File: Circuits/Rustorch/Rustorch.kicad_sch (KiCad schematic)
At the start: 0 parts

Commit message: (Rustorch) 回路図部品配置中
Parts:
- added BZ1: Buzzer, symbol Device:Buzzer
- added C1, C3: 0.1u, symbol Device:C_Small
- added C2: 47u, symbol Device:C_Polarized_Small
- added D1, D3, D4, D5: 1N4148, symbol Device:D_Small
- added D2: LED_POWER, symbol Device:LED_Small
- added J1: USB_C_Receptacle_USB2.0_16P, symbol Connector:USB_C_Receptacle_USB2.0_16P
- added J2: OLED_128x64_IIC, symbol Connector:Conn_01x04_Socket
- added Q1, Q2, Q3, Q4: 2SC1815, Package_TO_SOT_THT:TO-92_Inline, symbol Transistor_BJT:2SC1815
- added R1, R2, R4, R5, R6: 4.7k, symbol Device:R_Small
- added R10, R13, R14, R15, R16, R17, R18, R19: 330, symbol Device:R_Small
- added R3, R7, R8, R9: 10k, symbol Device:R_Small
- added SW1: RESET, symbol Switch:SW_Push
- added SW2: SW_UP, symbol Switch:SW_Push
- added SW3: SW_LEFT, symbol Switch:SW_Push
- added SW4: SW_RIGHT, symbol Switch:SW_Push
- added SW5: SW_DOWN, symbol Switch:SW_Push
- added SW6: SW_A, symbol Switch:SW_Push
- added SW7: SW_B, symbol Switch:SW_Push
- added SW8: BOOT, symbol Switch:SW_Push
- added SW9: SW_POWER (5P), symbol Switch:SW_Push_SPDT
- added U1: ESP32-C6-WROOM-1, PCM_Espressif:ESP32-C6-WROOM-1, symbol PCM_Espressif:ESP32-C6-WROOM-1
- added U2: BA033CC0T, Package_TO_SOT_THT:TO-220-3_Vertical, symbol Regulator_Linear:LF33_TO220
- added U3, U4, U5, U6: OSL10561-L*, Display_7Segment:7SegmentLED_LTS6760_LTS6780, symbol Display_Character:SM420561N
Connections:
- new net: C1.1, D1.1 (K), R3.2, SW9.2 (B), U2.1 (VI)
- new net: J1.B5 (CC2), R2.1
- new net: D2.2 (A), R3.1
- new net: BZ1.1 (+), R7.2
- new net: U1.1 (GND), U1.28 (GND), U1.29 (GND)
- new net: Q1.3 (B), R4.2
- new net: J1.A5 (CC1), R1.1
- new net 3V3: C2.1, C3.1, D1.2 (A), J2.2 (Pin_2), R5.2, R6.2, U2.3 (VO)
- new net GND: BZ1.2 (-), C1.2, C2.2, C3.2, D2.1 (K), J1.A1 (GND), J1.A12 (GND), J1.B1 (GND), J1.B12 (GND), J2.1 (Pin_1), Q1.1 (E), Q2.1 (E), Q3.1 (E), Q4.1 (E), R1.2, R2.2, U2.2 (GND)
- new net SCL: J2.3 (Pin_3), R6.1, U1.7 (MTDO/GPIO7)
- new net SDA: J2.4 (Pin_4), R5.1, U1.6 (MTCK/GPIO6/ADC1_CH6)
- new net USB_D+: J1.A6 (D+), J1.B6 (D+), U1.14 (GPIO13/USB_D+)
- new net USB_D-: J1.A7 (D-), J1.B7 (D-), U1.13 (GPIO12/USB_D-)
- new net VBUS: J1.A4 (VBUS), J1.A9 (VBUS), J1.B4 (VBUS), J1.B9 (VBUS), SW9.1 (A)
- no-connect marks 0 -> 4

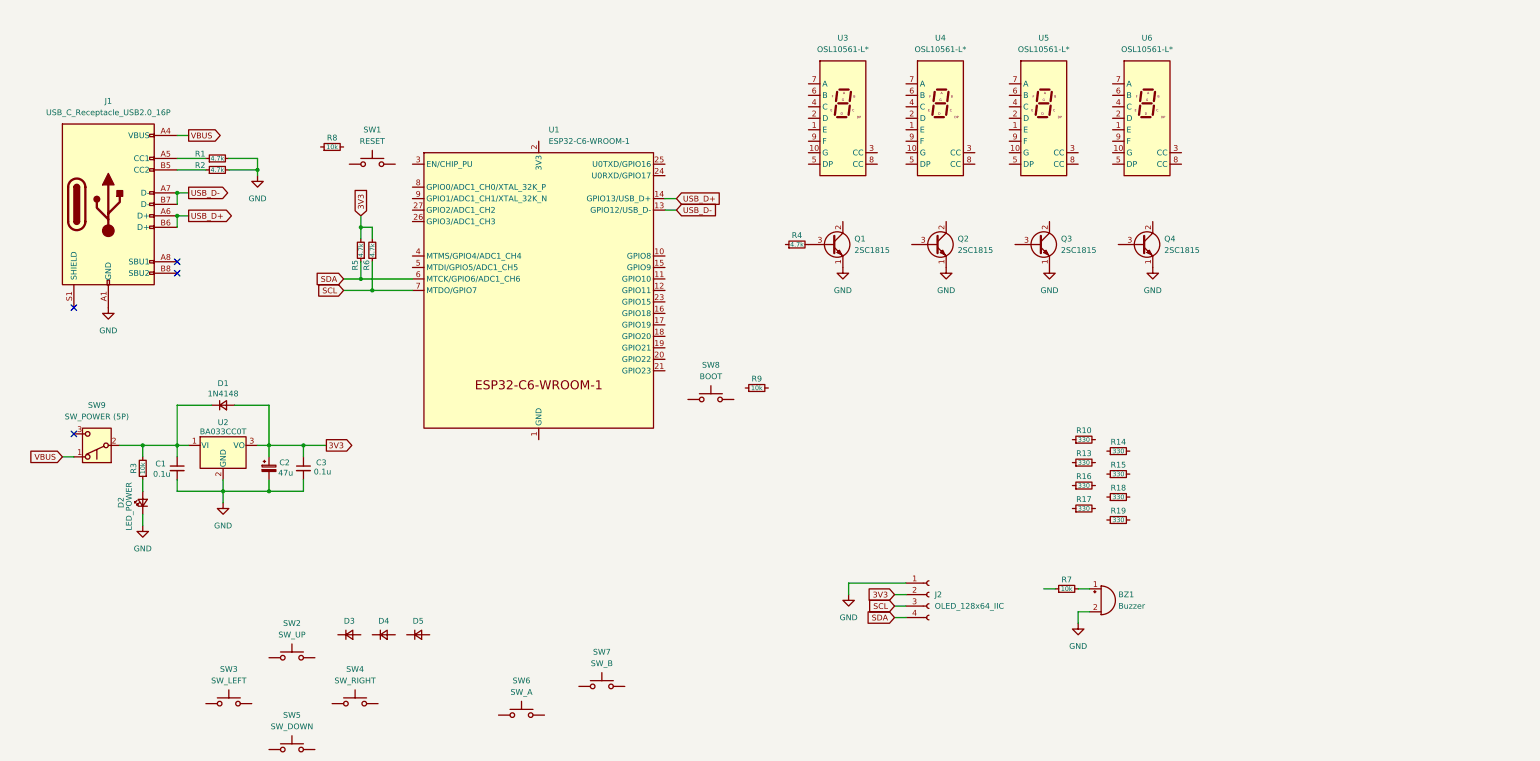
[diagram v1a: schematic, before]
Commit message: (Rustorch) 回路図修正 (7セグ部分追加)
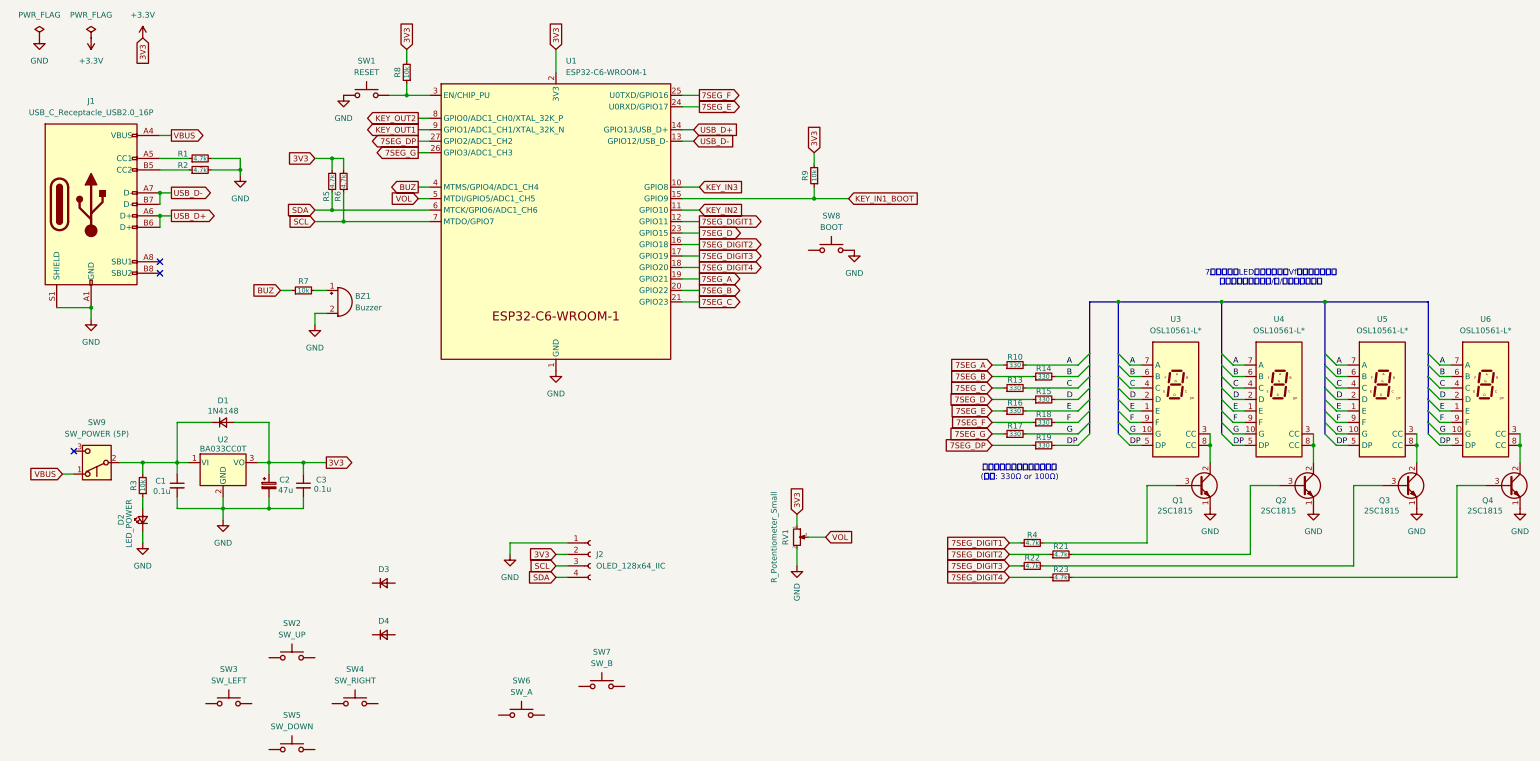
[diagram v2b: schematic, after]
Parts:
- removed D5: 1N4148, symbol Device:D_Small
- added R21, R22, R23: 4.7k, symbol Device:R_Small
- added RV1: R_Potentiometer_Small, symbol Device:R_Potentiometer_Small
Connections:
- net 3V3 is gone; now on net +3.3V: C2.1, C3.1, D1.2 (A), J2.2 (Pin_2), R5.2, R6.2, U2.3 (VO)
- net GND: now also J1.S1 (SHIELD), SW1.1, SW8.2, U1.1 (GND), U1.28 (GND), U1.29 (GND), RV1.3
- net at Q3.2 (C): now also U5.3 (CC), U5.8 (CC)
- net at Q3.3 (B): now also R22.2
- net at Q4.2 (C): now also U6.3 (CC), U6.8 (CC)
- net at Q4.3 (B): now also R23.2
- net E: now reaches U6.1 (E)
- net E: now also R16.2, U3.1 (E), U4.1 (E), U5.1 (E)
- net G: now reaches U6.10 (G)
- net G: now also R17.2, U3.10 (G), U4.10 (G), U5.10 (G)
- net D: now reaches U6.2 (D)
- net D: now also R15.2, U3.2 (D), U4.2 (D), U5.2 (D)
- net C: now reaches U6.4 (C)
- net C: now also R13.2, U3.4 (C), U4.4 (C), U5.4 (C)
- net DP: now reaches U6.5 (DP)
- net DP: now also R19.2, U3.5 (DP), U4.5 (DP), U5.5 (DP)
- net B: now reaches U6.6 (B)
- net B: now also R14.2, U3.6 (B), U4.6 (B), U5.6 (B)
- net A: now reaches U6.7 (A)
- net A: now also R10.2, U3.7 (A), U4.7 (A), U5.7 (A)
- net F: now reaches U6.9 (F)
- net F: now also R18.2, U3.9 (F), U4.9 (F), U5.9 (F)
- net 7SEG_G: now reaches R17.1
- net 7SEG_G: now also U1.26 (GPIO3/ADC1_CH3)
- net 7SEG_F: now reaches R18.1
- net 7SEG_F: now also U1.25 (U0TXD/GPIO16)
- net BUZ: now reaches R7.1
- net BUZ: now also U1.4 (MTMS/GPIO4/ADC1_CH4)
- net KEY_IN3: now reaches U1.10 (GPIO8)
- net KEY_IN2: now reaches U1.11 (GPIO10)
- net 7SEG_DIGIT1: now reaches U1.12 (GPIO11)
- net 7SEG_DIGIT1: now also R4.1
- net KEY_IN1_BOOT: now reaches U1.15 (GPIO9)
- net KEY_IN1_BOOT: now also R9.1
- net 7SEG_DIGIT2: now reaches U1.16 (GPIO18)
- net 7SEG_DIGIT2: now also R21.1
- net 7SEG_DIGIT3: now reaches U1.17 (GPIO19)
- net 7SEG_DIGIT3: now also R22.1
- net 7SEG_DIGIT4: now reaches U1.18 (GPIO20)
- net 7SEG_DIGIT4: now also R23.1
- net 7SEG_A: now reaches U1.19 (GPIO21)
- net 7SEG_A: now also R10.1
- net +3.3V: now reaches U1.2 (3V3)
- net +3.3V: now also R8.2, R9.2, RV1.1
- net 7SEG_B: now reaches U1.20 (GPIO22)
- net 7SEG_B: now also R14.1
- net 7SEG_C: now reaches U1.21 (GPIO23)
- net 7SEG_C: now also R13.1
- net 7SEG_D: now reaches U1.23 (GPIO15)
- net 7SEG_D: now also R15.1
- net 7SEG_E: now reaches U1.24 (U0RXD/GPIO17)
- net 7SEG_E: now also R16.1
- net 7SEG_DP: now reaches U1.27 (GPIO2/ADC1_CH2)
- net 7SEG_DP: now also R19.1
- net at U1.3 (EN/CHIP_PU): now also R8.1, SW1.2
- net VOL: now reaches U1.5 (MTDI/GPIO5/ADC1_CH5)
- net VOL: now also RV1.2
- net KEY_OUT2: now reaches U1.8 (GPIO0/ADC1_CH0/XTAL_32K_P)
- net KEY_OUT1: now reaches U1.9 (GPIO1/ADC1_CH1/XTAL_32K_N)
- net at Q1.2 (C): now also U3.3 (CC), U3.8 (CC)
- net at U4.3 (CC): now also Q2.2 (C), U4.8 (CC)
- net at Q2.3 (B): now also R21.2
- no-connect marks 4 -> 3
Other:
- note added: "7セグメントLEDの色は実際のVfを見つつ決める 基本的に赤想定で青/緑/白は厳しめかも"
- note added: "電流制限抵抗の抵抗値は暫定 (候補: 330Ω or 100Ω)"
- moved on the sheet: BZ1, C1, C2, C3, D1, D2, D3, J1, J2, Q1, R1, R10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

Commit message: (Rustorch) 回路図修正 (キーマトリクス追加)
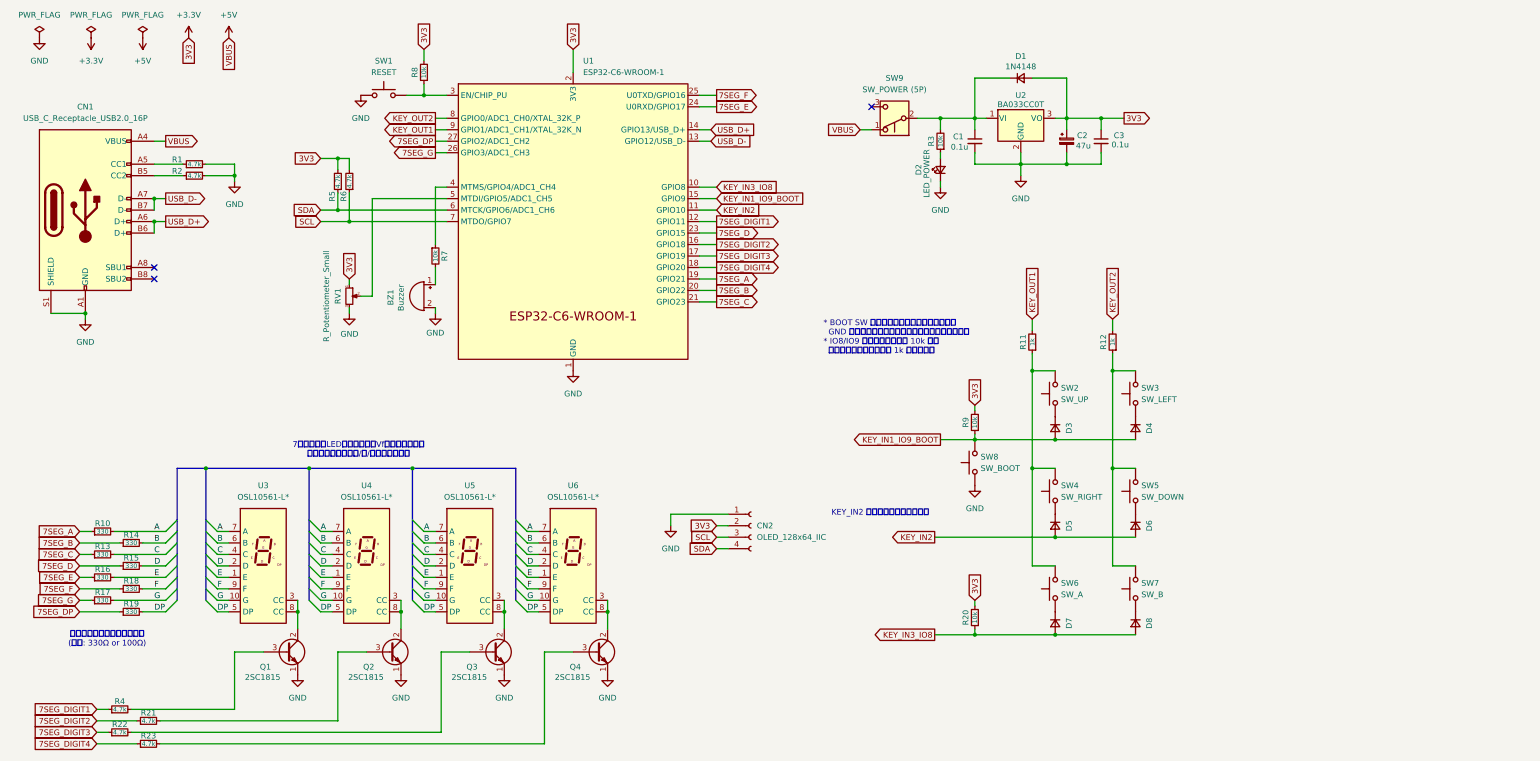
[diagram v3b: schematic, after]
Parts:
- added D5, D6, D7, D8: 1N4148, symbol Device:D_Small
- added R11, R12: 1k, symbol Device:R_Small
- added R20: 10k, symbol Device:R_Small
- SW8: value BOOT -> SW_BOOT
- renumbered J1 to CN1, J2 to CN2
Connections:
- net KEY_IN1_BOOT is gone; now on net KEY_IN1_IO9_BOOT: R9.1, U1.15 (GPIO9)
- net +3.3V: now also R20.2
- net GND: now also SW8.1; no longer SW8.2
- net KEY_IN2: now also D5.2 (A), D6.2 (A)
- net KEY_OUT1: now also R11.2
- net KEY_OUT2: now also R12.2
- net at SW4.1: now also D5.1 (K)
- net at SW4.2: now also SW2.2, SW6.2, R11.1
- net at D3.1 (K): now also SW2.1
- net KEY_IN1_IO9_BOOT: now reaches D3.2 (A)
- net KEY_IN1_IO9_BOOT: now also D4.2 (A), SW8.2
- net at SW3.1: now also D4.1 (K)
- net at SW3.2: now also SW5.2, SW7.2, R12.1
- net at SW6.1: now also D7.1 (K)
- net at SW7.1: now also D8.1 (K)
- net at SW5.1: now also D6.1 (K)
- net BUZ: no longer names the net of R7.1, U1.4 (MTMS/GPIO4/ADC1_CH4)
- net KEY_IN3 renamed KEY_IN3_IO8
- net KEY_IN3_IO8: now also D7.2 (A), D8.2 (A), R20.1
- net VBUS renamed +5V
- net VOL: no longer names the net of RV1.2, U1.5 (MTDI/GPIO5/ADC1_CH5)
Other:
- note added: "* BOOT SW 押下時にキースキャン用の出力が GND 直結になるのを防止する用に直列抵抗を入れる * IO8/IO9 のプルアップ抵抗 10k との 分圧を考えて直列抵抗は 1k にしておく"
- note added: "KEY_IN2 は内蔵プルアップを使用"
- moved on the sheet: BZ1, C1, C2, C3, CN1, CN2, D1, D2, D3, D4, Q1, Q2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

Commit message: (Rustorch) 回路図修正 (アノテーションのエラー/警告に対処)
* バス接続エラー：7SEG のバスにグループラベル {A B ... DP} を付与することで解決
* 電源ラベルエラー：グローバルラベル3V3 と電源の +3.3V が衝突していたので +3.3V に統一
* 電源出力衝突エラー：3端子レギュレータ VO に PWR_FLAG を付与した +3.3V を接続していてエラーになったので PWR_FLAG を除去
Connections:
- net +5V: now also C1.1, D1.1 (K), R3.2, SW9.2 (B), U2.1 (VI); no longer CN1.A4 (VBUS), CN1.A9 (VBUS), CN1.B4 (VBUS), CN1.B9 (VBUS), SW9.1 (A)
- new net VBUS: CN1.A4 (VBUS), CN1.A9 (VBUS), CN1.B4 (VBUS), CN1.B9 (VBUS), SW9.1 (A)
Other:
- moved on the sheet: CN2, Q1, Q2, Q3, Q4, R10, R13, R14, R15, R16, R17, R18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
